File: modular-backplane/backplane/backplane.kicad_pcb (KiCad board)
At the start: 4 copper layers, 100 x 100 mm, 84 parts, among them J1 West, J10 Module, J11 Module, J12 Module, J13 Module, J14 Module, J15 Module, J16 Module, J17 Module, J18 Module, J19 Module, J2 South, J20 Module, J21 Module, J22 Module, J23 Module, J24 Module, J25 Module, J26 Module, J27 Module, J28 Module, J29 Module, J3 North, J30 Module, J31 Module, J32 Module, J33 Module, J34 Module, J35 Module, J36 Module, J37 Module, J38 Module, J39 Module, J4 East, J40 Module, J41 Module, J42 Module, J43 Module, J44 Module, J45 Module, J46 Module, J47 Module, J48 Module, J49 Module, J50 Module, J51 Module, J52 Module, J53 Module, J54 Module, J55 Module, J56 Module, J57 Module, J58 Module, J59 Module, J60 Module, J61 Module, J62 Module, J63 Module, J64 Module, J65 Module, J66 Module, J67 Module, J68 Module, J69 Module, J70 Module, J71 Module, J72 Module, J9 Module, SW1 A, SW2 B, SW3 C, SW4 D, SW5 E, SW6 F, SW7 G, SW8 H, U1 74HC14, U2 74HC14, U3 VN5E160S

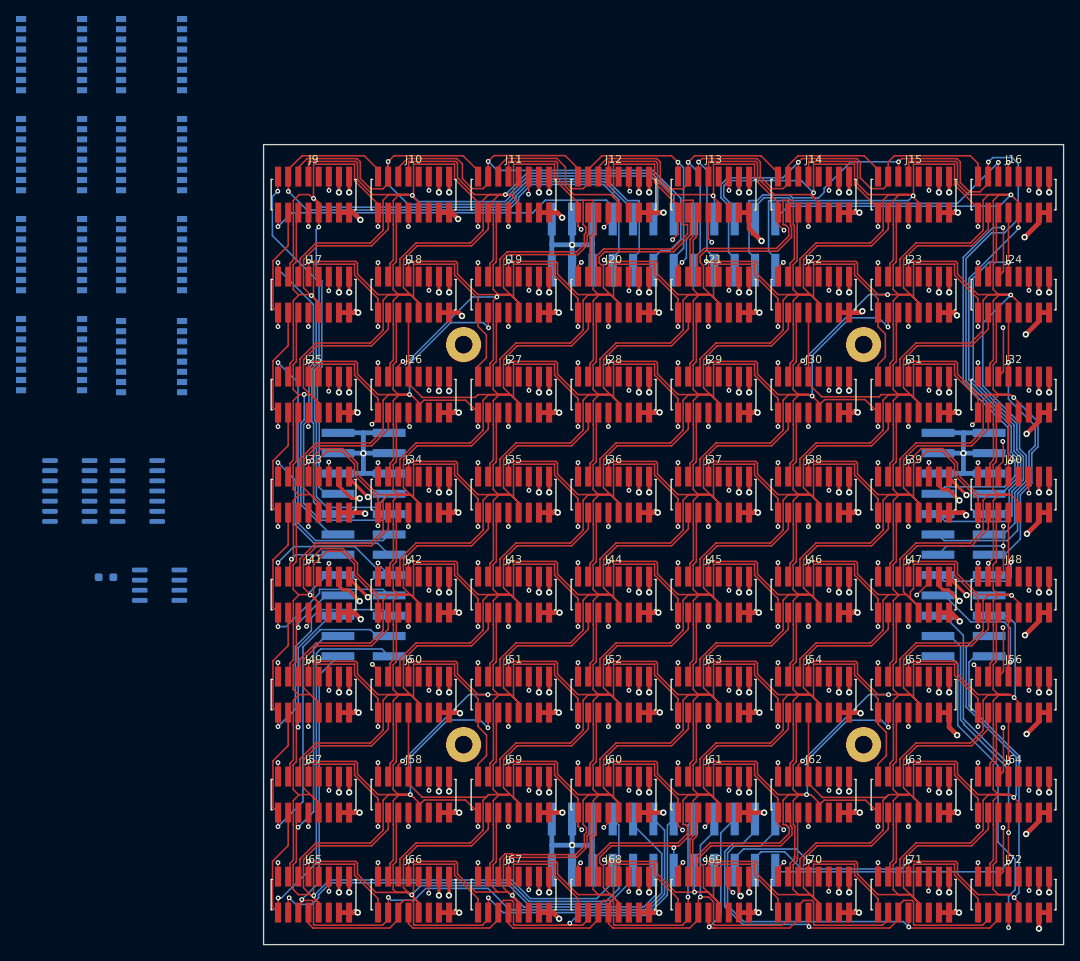
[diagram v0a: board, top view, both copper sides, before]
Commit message: Place and route DIP switches
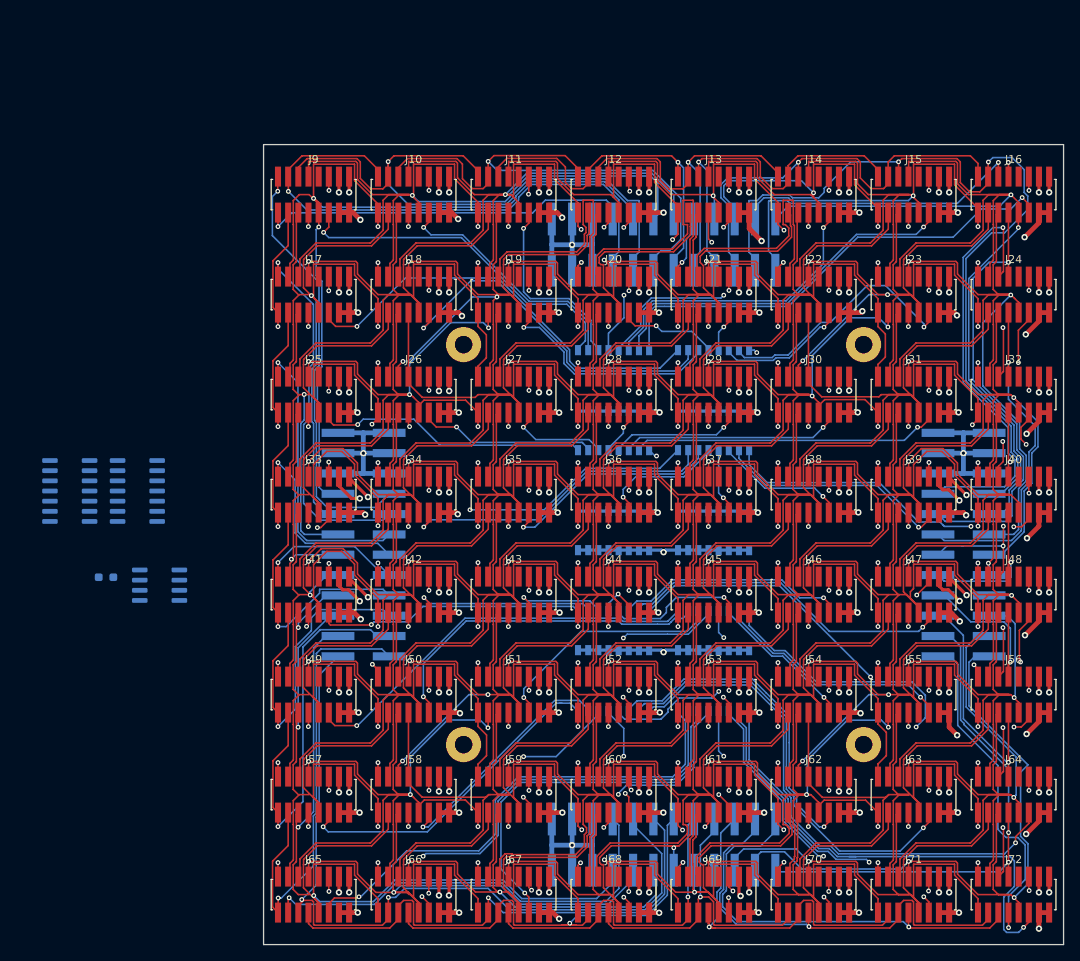
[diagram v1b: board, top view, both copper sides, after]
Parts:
- moved SW8 113.9 mm to (106.2, 117.0), turned to 0 degrees
- moved SW7 96.2 mm to (93.8, 117.0), turned to 0 degrees
- moved SW6 92.2 mm to (106.2, 104.5), turned to 0 degrees
- moved SW4 88.2 mm to (106.2, 92.0), turned to 0 degrees
- moved SW5 75.7 mm to (93.8, 104.5), turned to 0 degrees
- moved SW2 72.0 mm to (106.2, 79.5), turned to 0 degrees
- moved SW3 70.7 mm to (93.8, 92.0), turned to 0 degrees
- moved SW1 57.8 mm to (93.8, 79.5), turned to 0 degrees
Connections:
- SW5 pad 1: /T-E0 -> GND
- SW5 pad 10: GND -> /T-E6
- SW5 pad 11: GND -> /T-E5
- SW5 pad 12: GND -> /T-E4
- SW5 pad 13: GND -> /T-E3
- SW5 pad 14: GND -> /T-E2
- SW5 pad 15: GND -> /T-E1
- SW5 pad 16: GND -> /T-E0
- SW5 pad 2: /T-E1 -> GND
- SW5 pad 3: /T-E2 -> GND
- SW5 pad 4: /T-E3 -> GND
- SW5 pad 5: /T-E4 -> GND
- SW5 pad 6: /T-E5 -> GND
- SW5 pad 7: /T-E6 -> GND
- SW5 pad 8: /T-E7 -> GND
- SW5 pad 9: GND -> /T-E7
- SW6 pad 1: /T-F0 -> GND
- SW6 pad 10: GND -> /T-F6
- SW6 pad 11: GND -> /T-F5
- SW6 pad 12: GND -> /T-F4
- SW6 pad 13: GND -> /T-F3
- SW6 pad 14: GND -> /T-F2
- SW6 pad 15: GND -> /T-F1
- SW6 pad 16: GND -> /T-F0
- SW6 pad 2: /T-F1 -> GND
- SW6 pad 3: /T-F2 -> GND
- SW6 pad 4: /T-F3 -> GND
- SW6 pad 5: /T-F4 -> GND
- SW6 pad 6: /T-F5 -> GND
- SW6 pad 7: /T-F6 -> GND
- SW6 pad 8: /T-F7 -> GND
- SW6 pad 9: GND -> /T-F7
- SW7 pad 1: /T-G0 -> GND
- SW7 pad 10: GND -> /T-G6
- SW7 pad 11: GND -> /T-G5
- SW7 pad 12: GND -> /T-G4
- SW7 pad 13: GND -> /T-G3
- SW7 pad 14: GND -> /T-G2
- SW7 pad 15: GND -> /T-G1
- SW7 pad 16: GND -> /T-G0
- SW7 pad 2: /T-G1 -> GND
- SW7 pad 3: /T-G2 -> GND
- SW7 pad 4: /T-G3 -> GND
- SW7 pad 5: /T-G4 -> GND
- SW7 pad 6: /T-G5 -> GND
- SW7 pad 7: /T-G6 -> GND
- SW7 pad 8: /T-G7 -> GND
- SW7 pad 9: GND -> /T-G7
- SW8 pad 1: /T-H0 -> GND
- SW8 pad 10: GND -> /T-H6
- SW8 pad 11: GND -> /T-H5
- SW8 pad 12: GND -> /T-H4
- SW8 pad 13: GND -> /T-H3
- SW8 pad 14: GND -> /T-H2
- SW8 pad 15: GND -> /T-H1
- SW8 pad 16: GND -> /T-H0
- SW8 pad 2: /T-H1 -> GND
- SW8 pad 3: /T-H2 -> GND
- SW8 pad 4: /T-H3 -> GND
- SW8 pad 5: /T-H4 -> GND
- SW8 pad 6: /T-H5 -> GND
- SW8 pad 7: /T-H6 -> GND
- SW8 pad 8: /T-H7 -> GND
- SW8 pad 9: GND -> /T-H7
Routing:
- net GND: track 285.3 -> 369.5 mm, vias 68 -> 70
- net /T-G7: track 0.00 -> 67.6 mm, vias 0 -> 1
- net /T-H0: track 0.00 -> 62.5 mm, vias 0 -> 1
- net /T-H7: track 0.00 -> 60.9 mm, vias 0 -> 1
- net /T-E7: track 0.00 -> 60.0 mm, vias 0 -> 2
- net /T-A7: track 0.00 -> 59.5 mm, vias 0 -> 1
- net /T-C7: track 0.00 -> 55.6 mm, vias 0 -> 2
- net /T-G6: track 0.00 -> 55.3 mm, vias 0 -> 1
- net /T-H1: track 0.00 -> 54.6 mm, vias 0 -> 2
- net /T-B0: track 0.00 -> 53.8 mm, vias 0 -> 1
- net /T-D0: track 0.00 -> 51.9 mm, vias 0 -> 2
- net /T-F0: track 0.00 -> 51.1 mm, vias 0 -> 1
- net /T-F7: track 0.00 -> 49.2 mm, vias 0 -> 2
- net /T-H2: track 0.00 -> 48.2 mm, vias 0 -> 1
- net /T-A6: track 0.00 -> 46.4 mm, vias 0 -> 1
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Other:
- board text added: "0"
- board text added: "1"
- board text added: "2"
- board text added: "3"
- board text added: "4"
- board text added: "5"
- board text added: "6"
- board text added: "7"
- board text added: "A"
- board text added: "B"
- board text added: "C"
- board text added: "D"
- board text added: "E"
- board text added: "F"
- board text added: "G"
- board text added: "H"

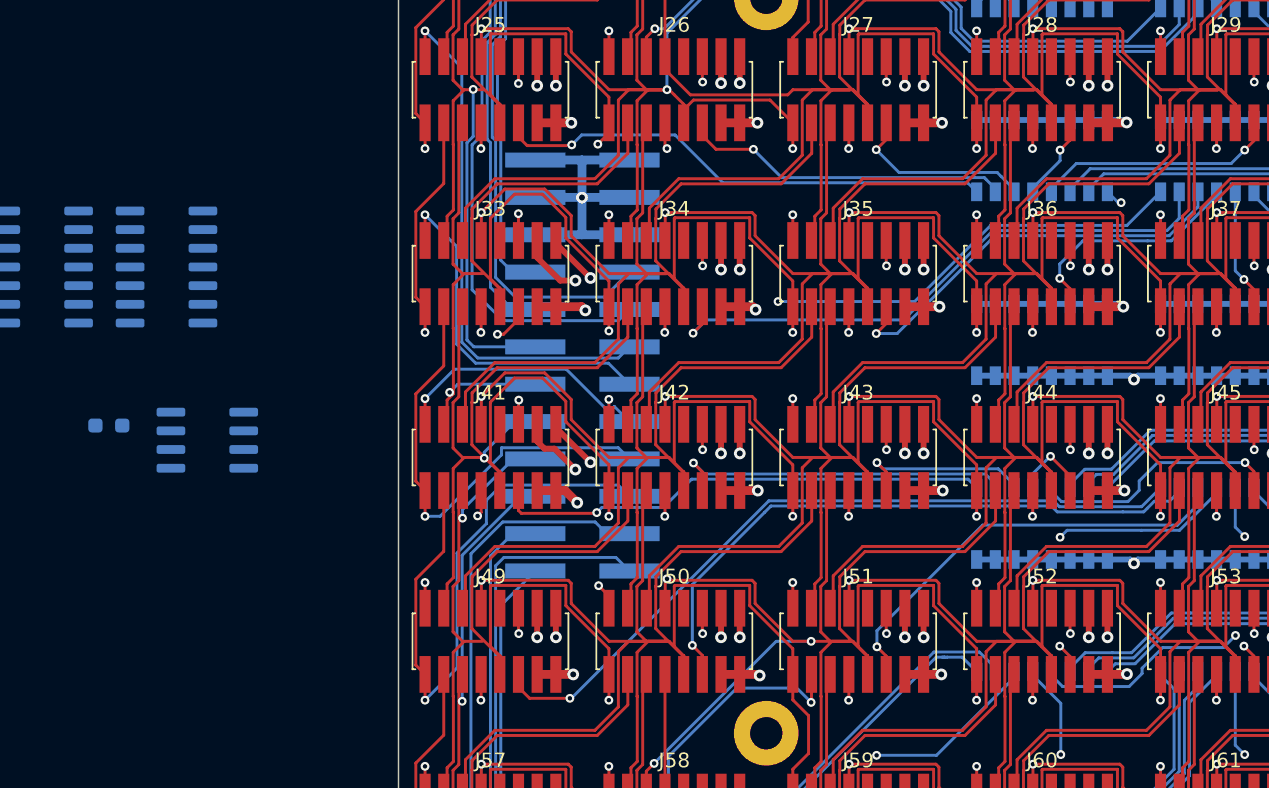
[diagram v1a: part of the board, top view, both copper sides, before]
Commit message: Place and route power/management connectors and power switch
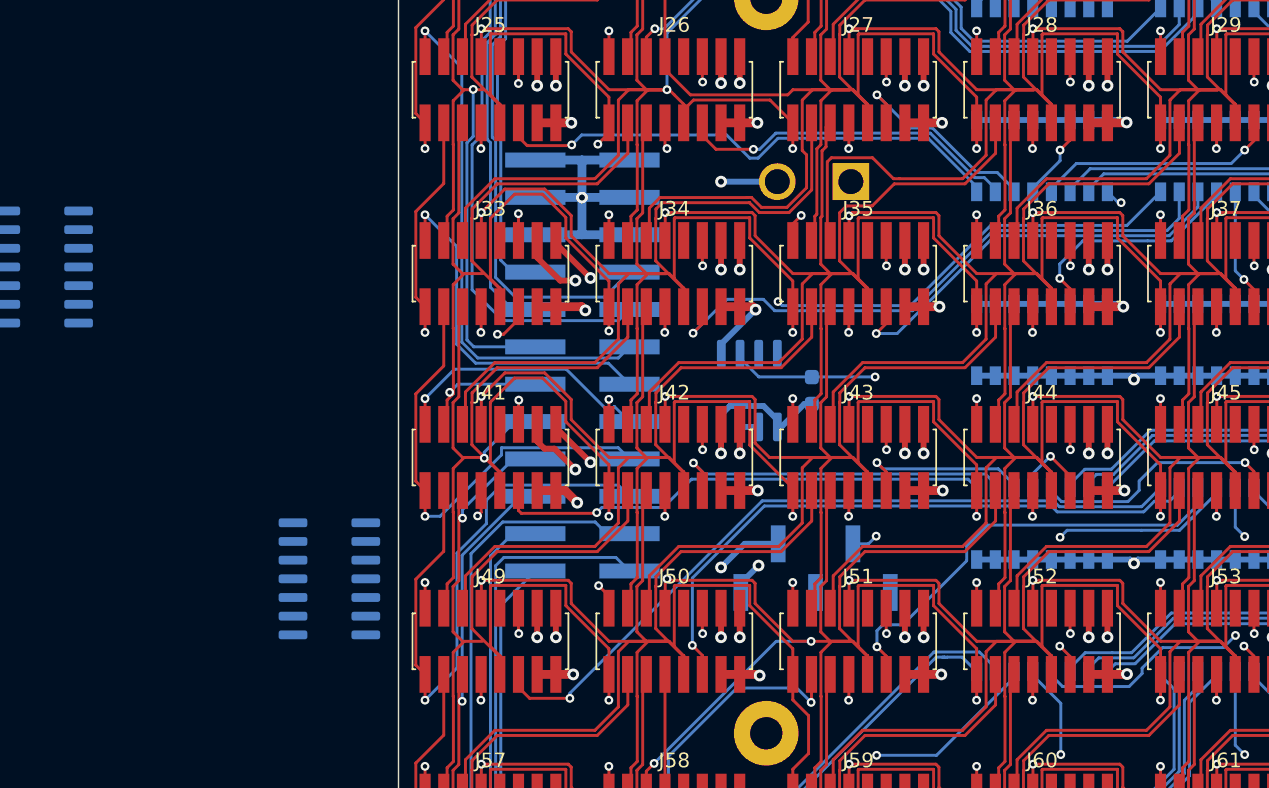
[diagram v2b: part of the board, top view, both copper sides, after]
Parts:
- added J5: 25-E900-02, agausmann:Conn_NTE_25-E900-02_01x02_P5.00mm_Vertical, B.Cu at (78.2, 87.5)
- added J6: MGMT, Connector_PinHeader_2.54mm:PinHeader_1x05_P2.54mm_Vertical_SMD_Pin1Right, B.Cu at (78.3, 113.8)
- moved R1 47.9 mm to (78.1, 101.7), turned to -90 degrees
- moved U3 37.0 mm to (73.8, 101.7), turned to -90 degrees
- moved U1 23.9 mm to (45.3, 114.5)
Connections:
- J10 pad 9: unconnected-(J10-Pad9) -> NRST
- J11 pad 9: unconnected-(J11-Pad9) -> NRST
- J12 pad 9: unconnected-(J12-Pad9) -> NRST
- J13 pad 9: unconnected-(J13-Pad9) -> NRST
- J14 pad 9: unconnected-(J14-Pad9) -> NRST
- J15 pad 9: unconnected-(J15-Pad9) -> NRST
- J16 pad 9: unconnected-(J16-Pad9) -> NRST
- J17 pad 9: unconnected-(J17-Pad9) -> NRST
- J18 pad 9: unconnected-(J18-Pad9) -> NRST
- J19 pad 9: unconnected-(J19-Pad9) -> NRST
- J20 pad 9: unconnected-(J20-Pad9) -> NRST
- J21 pad 9: unconnected-(J21-Pad9) -> NRST
- J22 pad 9: unconnected-(J22-Pad9) -> NRST
- J23 pad 9: unconnected-(J23-Pad9) -> NRST
- J24 pad 9: unconnected-(J24-Pad9) -> NRST
- J25 pad 9: unconnected-(J25-Pad9) -> NRST
- J26 pad 9: unconnected-(J26-Pad9) -> NRST
- J27 pad 9: unconnected-(J27-Pad9) -> NRST
- J28 pad 9: unconnected-(J28-Pad9) -> NRST
- J29 pad 9: unconnected-(J29-Pad9) -> NRST
- J30 pad 9: unconnected-(J30-Pad9) -> NRST
- J31 pad 9: unconnected-(J31-Pad9) -> NRST
- J32 pad 9: unconnected-(J32-Pad9) -> NRST
- J33 pad 9: unconnected-(J33-Pad9) -> NRST
- J34 pad 9: unconnected-(J34-Pad9) -> NRST
- J35 pad 9: unconnected-(J35-Pad9) -> NRST
- J36 pad 9: unconnected-(J36-Pad9) -> NRST
- J37 pad 9: unconnected-(J37-Pad9) -> NRST
- J38 pad 9: unconnected-(J38-Pad9) -> NRST
- J39 pad 9: unconnected-(J39-Pad9) -> NRST
- J40 pad 9: unconnected-(J40-Pad9) -> NRST
- J41 pad 9: unconnected-(J41-Pad9) -> NRST
- J42 pad 9: unconnected-(J42-Pad9) -> NRST
- J43 pad 9: unconnected-(J43-Pad9) -> NRST
- J44 pad 9: unconnected-(J44-Pad9) -> NRST
- J45 pad 9: unconnected-(J45-Pad9) -> NRST
- J46 pad 9: unconnected-(J46-Pad9) -> NRST
- J47 pad 9: unconnected-(J47-Pad9) -> NRST
- J48 pad 9: unconnected-(J48-Pad9) -> NRST
- J49 pad 9: unconnected-(J49-Pad9) -> NRST
- J50 pad 9: unconnected-(J50-Pad9) -> NRST
- J51 pad 9: unconnected-(J51-Pad9) -> NRST
- J52 pad 9: unconnected-(J52-Pad9) -> NRST
- J53 pad 9: unconnected-(J53-Pad9) -> NRST
- J54 pad 9: unconnected-(J54-Pad9) -> NRST
- J55 pad 9: unconnected-(J55-Pad9) -> NRST
- J56 pad 9: unconnected-(J56-Pad9) -> NRST
- J57 pad 9: unconnected-(J57-Pad9) -> NRST
- J58 pad 9: unconnected-(J58-Pad9) -> NRST
- J59 pad 9: unconnected-(J59-Pad9) -> NRST
- J60 pad 9: unconnected-(J60-Pad9) -> NRST
- J61 pad 9: unconnected-(J61-Pad9) -> NRST
- J62 pad 9: unconnected-(J62-Pad9) -> NRST
- J63 pad 9: unconnected-(J63-Pad9) -> NRST
- J64 pad 9: unconnected-(J64-Pad9) -> NRST
- J65 pad 9: unconnected-(J65-Pad9) -> NRST
- J66 pad 9: unconnected-(J66-Pad9) -> NRST
- J67 pad 9: unconnected-(J67-Pad9) -> NRST
- J68 pad 9: unconnected-(J68-Pad9) -> NRST
- J69 pad 9: unconnected-(J69-Pad9) -> NRST
- J70 pad 9: unconnected-(J70-Pad9) -> NRST
- J71 pad 9: unconnected-(J71-Pad9) -> NRST
- J72 pad 9: unconnected-(J72-Pad9) -> NRST
- J9 pad 9: unconnected-(J9-Pad9) -> NRST
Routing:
- net DIM: track 0.00 -> 23.0 mm, vias 0 -> 2
- net +5V: track 1612.1 -> 1631.1 mm, vias 64 -> 66
- net GND: track 369.5 -> 375.8 mm, vias 70 -> 71
- net /Cell-C3/STATE: track 120.3 -> 123.7 mm
- net VLED: track 1592.8 -> 1595.9 mm
- net /Cell-D3/STATE: track 120.3 -> 123.3 mm
- net /Cell-C2/STATE: track 119.5 -> 121.8 mm
- net /Cell-D1/STATE: track 121.6 -> 123.6 mm
- net /T-C2: track 12.8 -> 14.3 mm
- net /T-C0: track 34.3 -> 35.6 mm
- net /Cell-E2/STATE: track 120.3 -> 121.2 mm
- net /T-C1: track 22.5 -> 23.4 mm
- net /T-D1: track 40.1 -> 40.8 mm
- net /T-F2: track 29.8 -> 30.4 mm
